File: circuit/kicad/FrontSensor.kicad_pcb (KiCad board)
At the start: 2 copper layers, 70 x 30.3 mm, 18 parts, among them J1 FFC6, Q1 TEMT7100X01, Q2 TEMT7100X01, Q3 TEMT7100X01, Q4 TEMT7100X01

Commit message: サイドセンサのパターンは完成。メイン基板のフットプリント配置は完了。
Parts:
- moved R1 39.7 mm to (-13.0, -144.0), turned to 90 degrees
- moved R3 39.6 mm to (2.00, -145.0), turned to 90 degrees
- moved D4 36.4 mm to (-53.0, -149.0)
- moved D1 35.8 mm to (-48.0, -152.0)
- moved D2 32.5 mm to (-42.0, -152.0), turned to 270 degrees
- moved D3 30.8 mm to (-48.0, -146.0)
- moved Q4 25.2 mm to (27.3, -137.3), turned to 78.7 degrees
- moved Q2 11.7 mm to (-9.16, -139.7), turned to 93.7 degrees
- moved Q3 11.7 mm to (9.16, -139.7), turned to 86.2 degrees
- moved Q1 11.2 mm to (-9.81, -137.3), turned to 101.2 degrees
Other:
- board size 70 x 30.3 mm -> 50 x 32.5 mm

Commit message: hoge
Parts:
- D1, D2, D3, D4, Q1, Q2, Q3, Q4: moved to B.Cu
- moved R4 67.5 mm to (17.0, -149.0), turned to 173.4 degrees
- moved D4 64.6 mm to (11.5, -151.6), turned to 355.6 degrees
- moved R8 59.6 mm to (17.0, -151.0), turned to 173.5 degrees
- moved R2 56.3 mm to (-2.00, -150.0), turned to 180.7 degrees
- moved D3 55.8 mm to (7.50, -151.8), turned to 177.1 degrees
- moved R7 53.6 mm to (2.00, -152.0), turned to 359.2 degrees
- moved C1 45.1 mm to (5.00, -142.0)
- moved R6 43.5 mm to (-2.00, -152.0), turned to 179.2 degrees
- moved R5 39.7 mm to (-17.0, -151.0), turned to 6.4 degrees
- moved D1 36.5 mm to (-11.5, -151.6), turned to 184.3 degrees
- moved D2 34.5 mm to (-7.50, -151.8), turned to 2.8 degrees
- moved Q4 20.0 mm to (11.5, -149.6), turned to 175.6 degrees
- moved Q1 12.4 mm to (-11.5, -149.6), turned to 4.3 degrees
- moved Q2 10.2 mm to (-7.50, -149.8), turned to 182.8 degrees
- moved Q3 10.2 mm to (7.50, -149.8), turned to 357.1 degrees
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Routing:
- net +3V3: track 0.00 -> 68.9 mm, vias 0 -> 3
- net Net-(J1-Pad5): track 0.00 -> 20.3 mm, vias 0 -> 2
- net Net-(J1-Pad2): track 0.00 -> 20.3 mm, vias 0 -> 2
- net Net-(J1-Pad4): track 0.00 -> 15.1 mm, vias 0 -> 1
- net Net-(J1-Pad3): track 0.00 -> 15.0 mm, vias 0 -> 1
- net Net-(D1-Pad2): track 0.00 -> 4.05 mm, vias 0 -> 1
- net Net-(D4-Pad2): track 0.00 -> 4.05 mm, vias 0 -> 1
- net Net-(D3-Pad2): track 0.00 -> 3.96 mm, vias 0 -> 1
- net Net-(D2-Pad2): track 0.00 -> 3.95 mm, vias 0 -> 1
- net GND: track 0.00 -> 2.06 mm, vias 0 -> 4
- added copper zone on B.Cu, net GND
- added copper zone on F.Cu, net GND

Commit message: hoge
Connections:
- J1 pad MP: (no net) -> GND

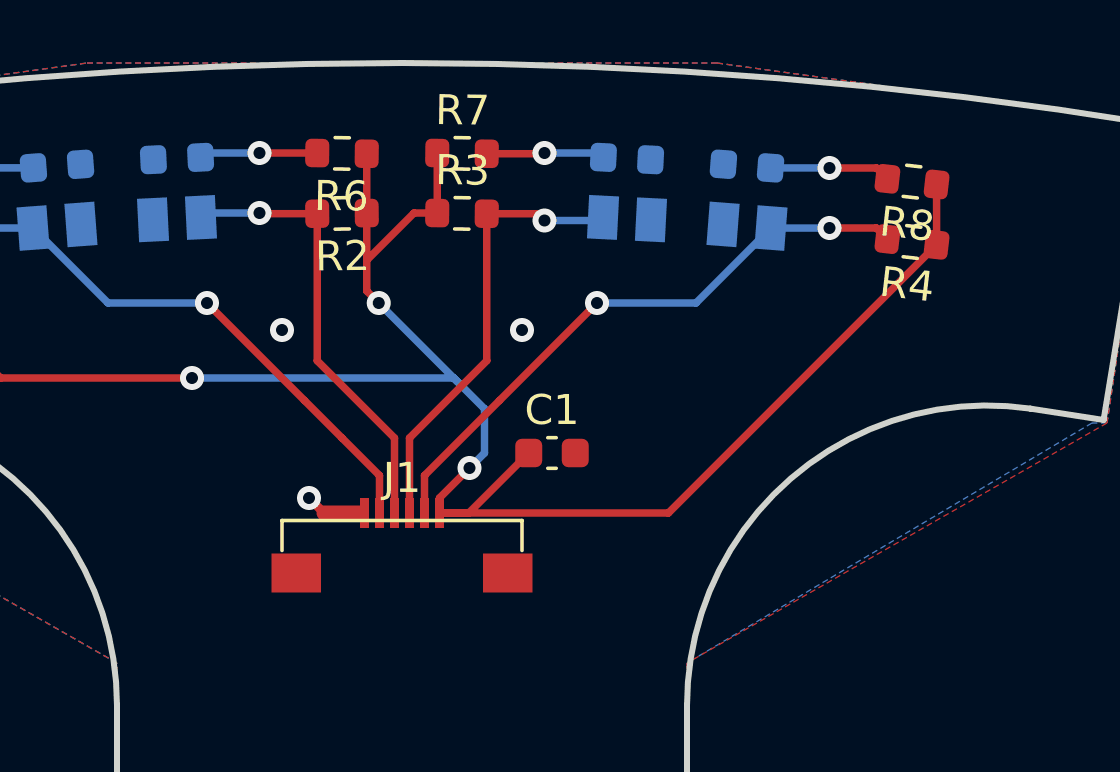
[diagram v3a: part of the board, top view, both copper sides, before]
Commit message: あとはシルクを見やすい位置にもっていくだけ。
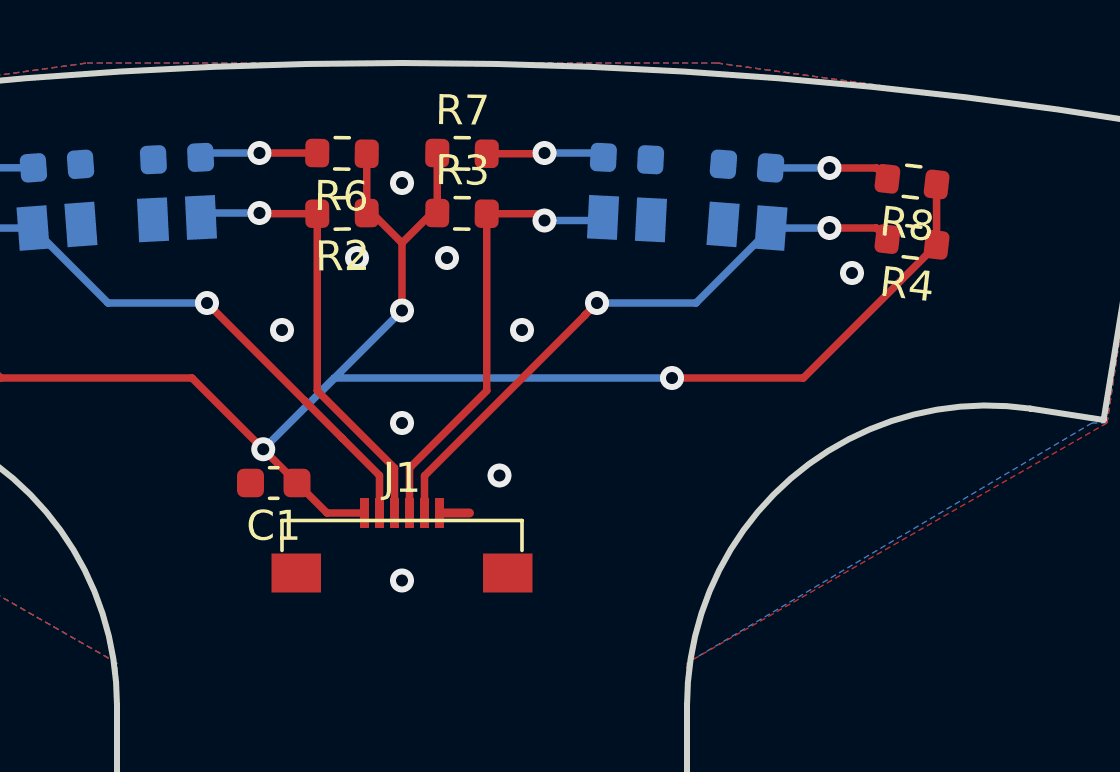
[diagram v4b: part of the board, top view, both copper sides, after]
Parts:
- moved C1 9.33 mm to (-4.28, -141.0), turned to 180 degrees
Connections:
- J1 pad 1: GND -> +3V3
- J1 pad 6: +3V3 -> GND
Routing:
- net +3V3: track 68.9 -> 62.9 mm
- net GND: track 1.96 -> 1.00 mm, vias 4 -> 10
